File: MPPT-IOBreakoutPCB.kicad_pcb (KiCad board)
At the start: 2 copper layers, 4 parts, among them J3 Conn_01x06, J4 Conn_01x06, J5 Conn_01x06

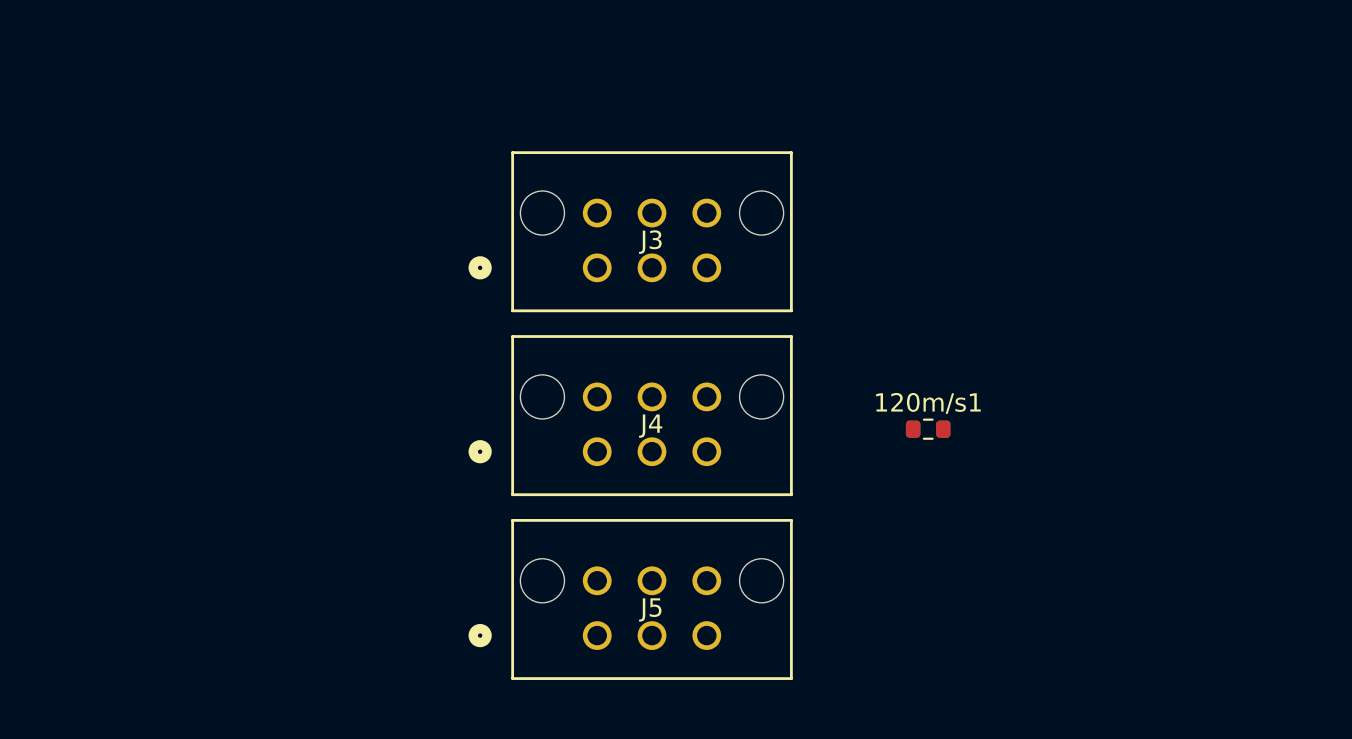
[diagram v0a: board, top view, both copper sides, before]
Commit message: mppt matched schem
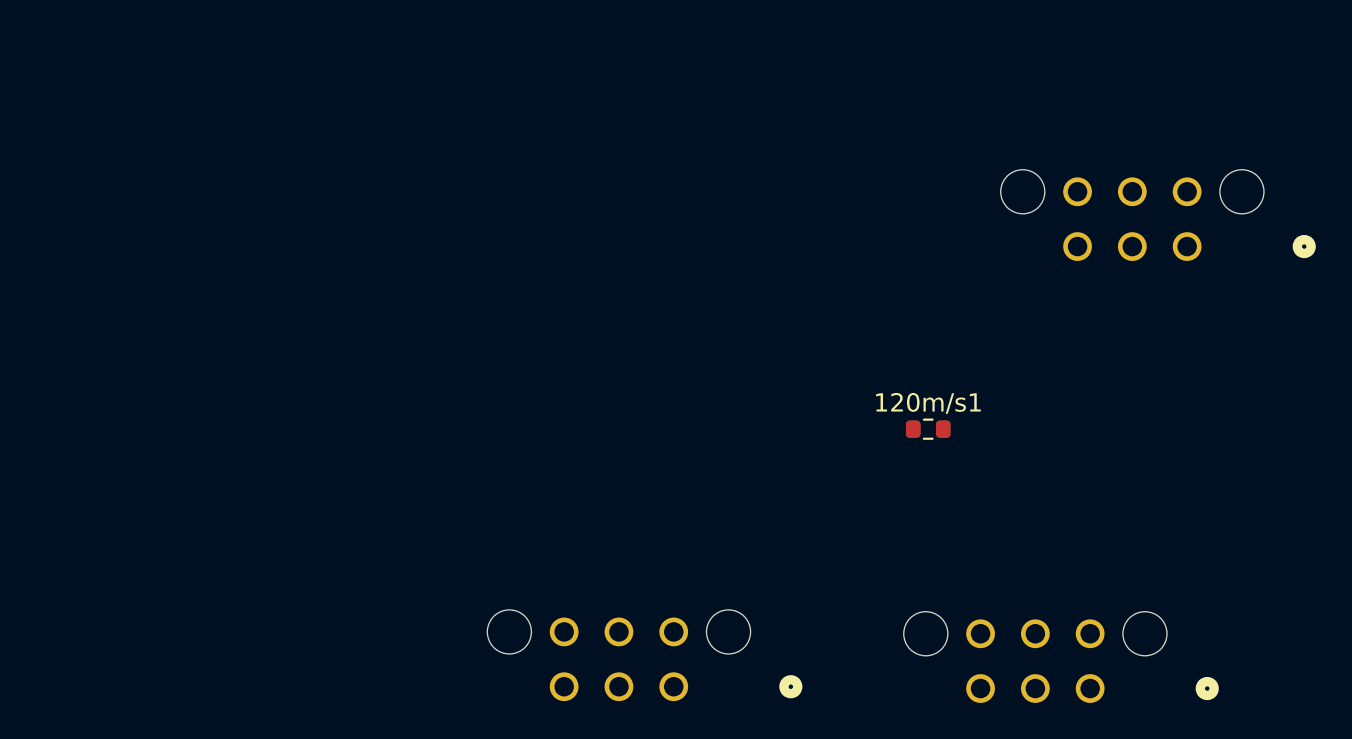
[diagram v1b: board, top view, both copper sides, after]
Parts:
- J1: renamed from J3; moved to B.Cu
- J2: renamed from J4; moved to B.Cu
- J3: renamed from J5; moved to B.Cu
- moved J3 38.7 mm to (164.6, 92.0), turned to 180 degrees
- moved J1 35.5 mm to (159.3, 116.2), turned to 180 degrees
- moved J2 13.5 mm to (136.5, 116.1), turned to 180 degrees
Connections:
- J2 pad 1: unconnected-(J4-Pin_1-Pad1) -> +12V
- J2 pad 2: unconnected-(J4-Pin_2-Pad2) -> GND
- J2 pad 4: /CAN_H-out -> /CAN_H-in
- J2 pad 5: /CAN_L-out -> /CAN_L-in

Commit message: layout maybe done
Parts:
- added REF**: MountingHole_3.2mm_M3, MountingHole:MountingHole_3.2mm_M3, F.Cu at (123.5, 87.7)
- J3: footprint UTSVT_Connectors:Molex_Microfit3.0_02x03_6-Pin-Vertical-PCB-Receptacle_447690601 -> footprints:CONN_SD-44764-001_06_MOL
- moved J2 32.6 mm to (113.8, 92.7)
- moved J1 31.2 mm to (138.8, 92.7)
- moved 120m/s1 20.3 mm to (139.7, 84.8)
- moved J3 16.9 mm to (148.1, 88.5), turned to 0 degrees
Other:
- board outline added: 54.8 x 15.3 mm
- board text added: "For Instructional Use Only."
- board text added: "SOLIDWORKS Educational Product."

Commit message: traces
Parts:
- moved 120m/s1 28.4 mm to (111.3, 84.4), turned to 180 degrees
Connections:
- J2 pad 4: /CAN_H-in -> /CAN_H-out
- J2 pad 5: /CAN_L-in -> /CAN_L-out
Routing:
- net /CAN_L-out: track 0.00 -> 53.0 mm
- net /CAN_H-out: track 0.00 -> 47.4 mm
- net /CAN_H-in: track 0.00 -> 17.0 mm
- net /CAN_L-in: track 0.00 -> 13.0 mm
- added copper zone on F.Cu, net +12V
- added copper zone on B.Cu, net GND
